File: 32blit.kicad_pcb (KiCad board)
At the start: 4 copper layers, 150 x 65 mm, 121 parts, among them CN1 LIPO BATTERY, J1 1X02PICOBLADE, J3 1X02JST_SH, Q5 DMN3023L, U1 SN74AHC1G02, U11 BQ24295, U22 MT25QL256ABA1EW7-0SIT, U3 AP3031KTR-G1 - ref 200mV, U4 ACCEL_LIS3DHTR, U5 PAM8301, U6 AP2112, U8 74VHC4053AFT, X1 MicroSD

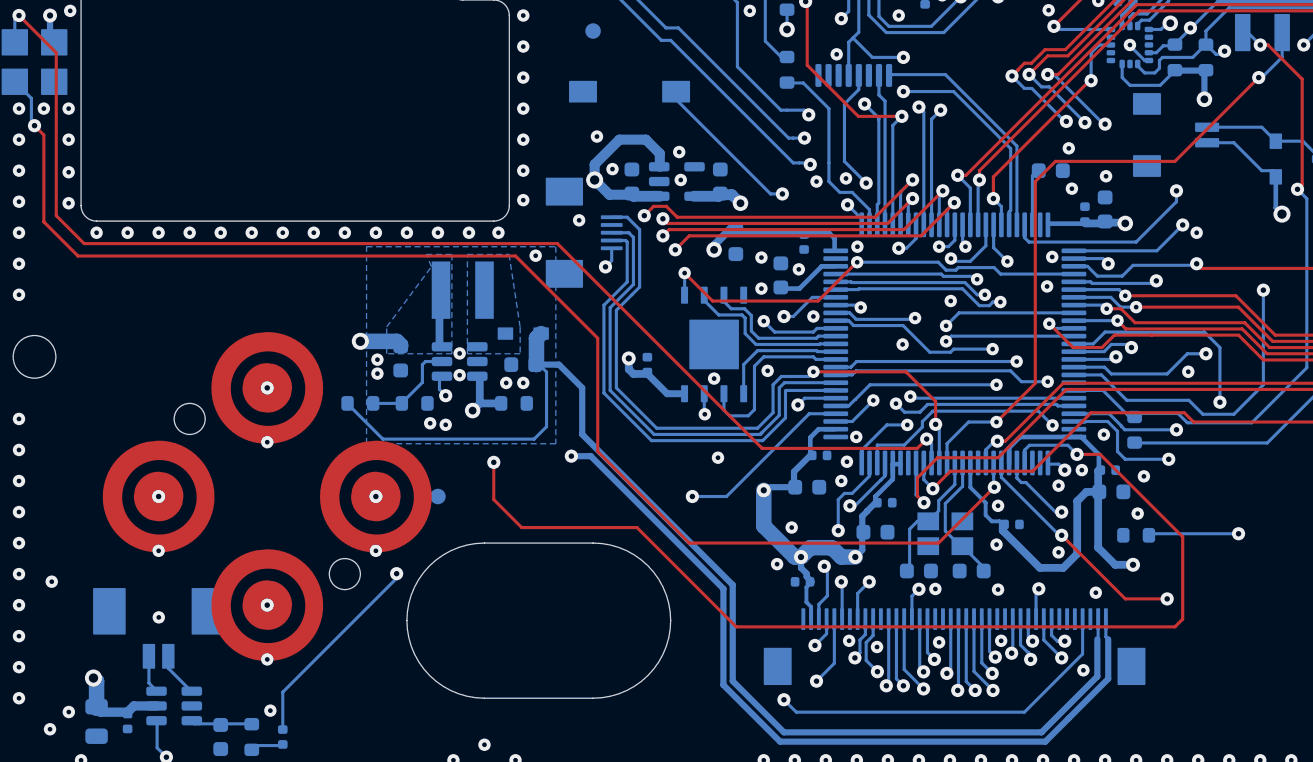
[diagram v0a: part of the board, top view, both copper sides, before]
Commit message: Replace speaker/vibration connector footprints
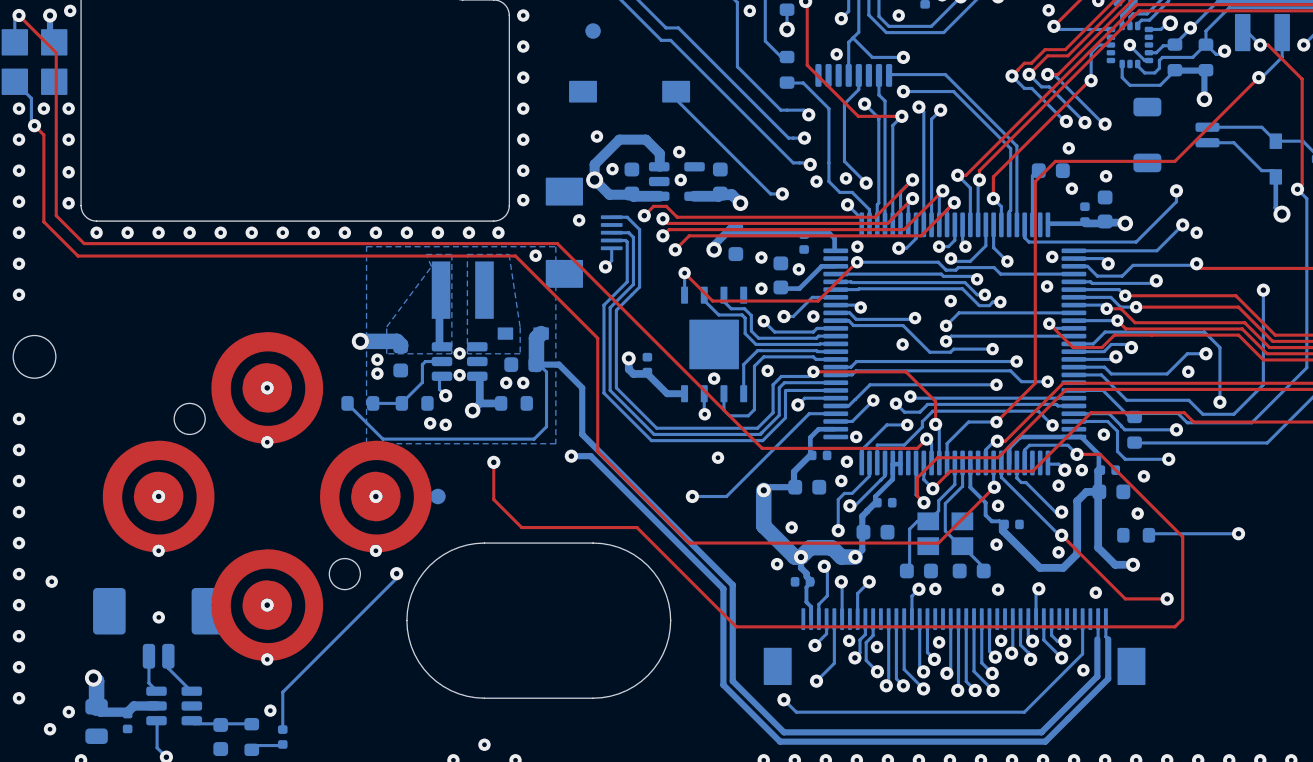
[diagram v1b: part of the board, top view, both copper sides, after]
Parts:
- J1: footprint 32blit:PICOBLADE_1.25MM_2P -> Connector_Molex:Molex_PicoBlade_53261-0271_1x02-1MP_P1.25mm_Horizontal
- J3: footprint 32blit:JST_SH_1.0MM_2P -> Connector_JST:JST_SH_SM02B-SRSS-TB_1x02-1MP_P1.00mm_Horizontal
- moved J3 2.80 mm to (150.1, 91.2)
- moved J1 1.60 mm to (84.5, 122.4)

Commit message: Giant schematic rework
Use as many kicad symbols as possiblem, adjust remaining imported symbols to make ERC happy and adjust some footprints for the new symbols
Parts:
- U4: value ACCEL_LIS3DHTR -> LIS3DHTR
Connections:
- net ACCEL_INT renamed /MCU/ACCEL_INT
- net AJOY_BUTTON renamed /MCU/AJOY_BUTTON
- net AJOY_LR renamed /MCU/AJOY_LR
- net AJOY_UD renamed /MCU/AJOY_UD
- net BATSENSE renamed /LCDs and Power/BATSENSE
- net DAC_AUDIO_OUT renamed /MCU/DAC_AUDIO_OUT
- net DPAD_DOWN renamed /MCU/DPAD_DOWN
- net DPAD_LEFT renamed /MCU/DPAD_LEFT
- net DPAD_RIGHT renamed /MCU/DPAD_RIGHT
- net DPAD_UP renamed /MCU/DPAD_UP
- net FLASH_CS renamed /MCU/FLASH_CS
- net FLASH_D0 renamed /MCU/FLASH_D0
- net FLASH_D1 renamed /MCU/FLASH_D1
- net FLASH_D2 renamed /MCU/FLASH_D2
- net FLASH_D3 renamed /MCU/FLASH_D3
- net FLASH_SCK renamed /MCU/FLASH_SCK
- net LCD_B2 renamed /LCDs and Power/LCD_B2
- net LCD_B3 renamed /LCDs and Power/LCD_B3
- net LCD_B4 renamed /LCDs and Power/LCD_B4
- net LCD_B5 renamed /LCDs and Power/LCD_B5
- net LCD_B6 renamed /LCDs and Power/LCD_B6
- net LCD_B7 renamed /LCDs and Power/LCD_B7
- net LCD_BACKLIGHT_EN renamed /LCDs and Power/LCD_BACKLIGHT_EN
- net LCD_CLK renamed /LCDs and Power/LCD_CLK
- net LCD_CS renamed /LCDs and Power/LCD_CS
- net LCD_DE renamed /LCDs and Power/LCD_DE
- net LCD_G2 renamed /LCDs and Power/LCD_G2
- net LCD_G3 renamed /LCDs and Power/LCD_G3
- net LCD_G4 renamed /LCDs and Power/LCD_G4
- net LCD_G5 renamed /LCDs and Power/LCD_G5
- net LCD_G6 renamed /LCDs and Power/LCD_G6
- net LCD_G7 renamed /LCDs and Power/LCD_G7
- net LCD_HSYNC renamed /LCDs and Power/LCD_HSYNC
- net LCD_R2 renamed /LCDs and Power/LCD_R2
- net LCD_R3 renamed /LCDs and Power/LCD_R3
- net LCD_R4 renamed /LCDs and Power/LCD_R4
- net LCD_R5 renamed /LCDs and Power/LCD_R5
- net LCD_R6 renamed /LCDs and Power/LCD_R6
- net LCD_R7 renamed /LCDs and Power/LCD_R7
- net LCD_RESET renamed /LCDs and Power/LCD_RESET
- net LCD_SPI_MOSI renamed /LCDs and Power/LCD_SPI_MOSI
- net LCD_SPI_SCLK renamed /LCDs and Power/LCD_SPI_SCLK
- net LCD_VSYNC renamed /LCDs and Power/LCD_VSYNC
- net LED_BLUE renamed /MCU/LED_BLUE
- net LED_CHG_BLUE renamed /LCDs and Power/LED_CHG_BLUE
- net LED_CHG_GREEN renamed /LCDs and Power/LED_CHG_GREEN
- net LED_CHG_RED renamed /LCDs and Power/LED_CHG_RED
- net LED_GREEN renamed /MCU/LED_GREEN
- net LED_RED renamed /MCU/LED_RED
- net SD_CS renamed /MCU/SD_CS
- net SD_SPI_MISO renamed /MCU/SD_SPI_MISO
- net SD_SPI_MOSI renamed /MCU/SD_SPI_MOSI
- net SD_SPI_SCLK renamed /MCU/SD_SPI_SCLK
- net SWA renamed /MCU/SWA
- net SWB renamed /MCU/SWB
- net SWHOME renamed /SWHOME
- net SWMENU renamed /MCU/SWMENU
- net VIBE_EN renamed /MCU/VIBE_EN
- net ~{AMP_SD} renamed /MCU/~{AMP_SD}
- C10 pad 1: 3V3 -> +3.3V
- C11 pad 1: 3V3 -> +3.3V
- C17 pad 1: 3V3 -> +3.3V
- C20 pad 1: 3V3 -> +3.3V
- C25 pad 1: 3V3 -> +3.3V
- C26 pad 1: 3V3 -> +3.3V
- C29 pad 1: 3V3 -> +3.3V
- C30 pad 1: 3V3 -> +3.3V
- C32 pad 1: 3V3 -> +3.3V
- C33 pad 1: 3V3 -> +3.3V
- C34 pad 1: 3V3 -> +3.3V
- C39 pad 1: USB_5V -> VBUS
- C4 pad 1: 3V3 -> +3.3V
- C5 pad 1: 3V3 -> +3.3V
- C6 pad 1: 3V3 -> +3.3V
- C7 pad 1: 3V3 -> +3.3V
- C8 pad 1: 3V3 -> +3.3V
- C9 pad 1: 3V3 -> +3.3V
- CN1 pad MP: (no net) -> unconnected-(CN1-MountPin-PadMP)
- FPC2 pad 2: 3V3 -> +3.3V
- J1 pad MP: (no net) -> GND
- J3 pad 1: 3V3 -> +3.3V
- J3 pad 2: Net-(Q5-D) -> Net-(D1-A)
- J3 pad MP: (no net) -> GND
- JOYSTICK0 pad 5: 3V3 -> +3.3V
- L2 pad 2: Net-(U3-SW) -> Net-(D2-A)
- Q5 pad 3: Net-(Q5-D) -> Net-(D1-A)
- R1 pad 2: 3V3 -> +3.3V
- R13 pad 2: 3V3 -> +3.3V
- R19 pad 1: I2C_SCL -> /I2C_SCL
- R19 pad 2: 3V3 -> +3.3V
- R20 pad 1: I2C_SDA -> /I2C_SDA
- R20 pad 2: 3V3 -> +3.3V
- R21 pad 1: USB_5V -> VBUS
- R29 pad 2: 3V3 -> +3.3V
- RGB1 pad 2: 3V3 -> +3.3V
- RGB2 pad 2: 3V3 -> +3.3V
- SJ1 pad 2: USB_5V -> VBUS
- STM32H750 pad 100: 3V3 -> +3.3V
- STM32H750 pad 11: 3V3 -> +3.3V
- STM32H750 pad 20: 3V3 -> +3.3V
- STM32H750 pad 21: 3V3 -> +3.3V
- STM32H750 pad 27: 3V3 -> +3.3V
- STM32H750 pad 50: 3V3 -> +3.3V
- STM32H750 pad 51: USB_ID -> /LCDs and Power/USB_ID
- STM32H750 pad 58: SD_DETECT -> /MCU/SD_DETECT
- STM32H750 pad 59: I2C_SCL -> /I2C_SCL
- STM32H750 pad 6: 3V3 -> +3.3V
- STM32H750 pad 60: I2C_SDA -> /I2C_SDA
- STM32H750 pad 75: 3V3 -> +3.3V
- SWRESET0 pad 2: /MCU/~{RESET} -> GND
- U$19 pad 2: Net-(U$19-GND-Pad2) -> unconnected-(U$19-Pad2)
- U$19 pad 4: Net-(U$19-GND-Pad2) -> unconnected-(U$19-Pad4)
- U1 pad 5: 3V3 -> +3.3V
- U11 pad 1: USB_5V -> VBUS
- U11 pad 2: USB_DP -> /LCDs and Power/USB_DP
- U11 pad 24: USB_5V -> VBUS
- U11 pad 3: USB_DM -> /LCDs and Power/USB_DM
- U11 pad 5: I2C_SCL -> /I2C_SCL
- U11 pad 6: I2C_SDA -> /I2C_SDA
- U22 pad 8: 3V3 -> +3.3V
- U3 pad 1: Net-(U3-SW) -> Net-(D2-A)
- U4 pad 1: 3V3 -> +3.3V
- U4 pad 14: 3V3 -> +3.3V
- U4 pad 4: I2C_SCL -> /I2C_SCL
- U4 pad 6: I2C_SDA -> /I2C_SDA
- U4 pad 8: 3V3 -> +3.3V
- U6 pad 4: (no net) -> unconnected-(U6-NC-Pad4)
- U6 pad 5: 3V3 -> +3.3V
- U8 pad 14: USB_DM -> /LCDs and Power/USB_DM
- U8 pad 15: USB_DP -> /LCDs and Power/USB_DP
- U8 pad 16: 3V3 -> +3.3V
- X1 pad 4: 3V3 -> +3.3V
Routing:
- net 3V3: track 145.6 -> 0.00 mm, vias 24 -> 0
- net +3.3V: track 0.00 -> 145.6 mm, vias 0 -> 24
- net VBUS: track 0.00 -> 85.1 mm, vias 0 -> 2
- net USB_5V: track 85.1 -> 0.00 mm, vias 2 -> 0
- net I2C_SDA: track 74.7 -> 0.00 mm, vias 4 -> 0
- net /I2C_SDA: track 0.00 -> 74.7 mm, vias 0 -> 4
- net I2C_SCL: track 71.3 -> 0.00 mm, vias 4 -> 0
- net /I2C_SCL: track 0.00 -> 71.3 mm, vias 0 -> 4
- net USB_DM: track 66.0 -> 0.00 mm
- net /LCDs and Power/USB_DM: track 0.00 -> 66.0 mm
- net USB_DP: track 65.0 -> 0.00 mm, vias 2 -> 0
- net /LCDs and Power/USB_DP: track 0.00 -> 65.0 mm, vias 0 -> 2
- net USB_ID: track 35.6 -> 0.00 mm, vias 2 -> 0
- net /LCDs and Power/USB_ID: track 0.00 -> 35.6 mm, vias 0 -> 2
- net SD_DETECT: track 21.2 -> 0.00 mm, vias 2 -> 0
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- added copper zone on In1.Cu, net +3.3V
- added copper zone on B.Cu, net Net-(D2-A)
- added copper zone on B.Cu, net VBUS
- removed copper zone on In1.Cu, net 3V3
- removed copper zone on B.Cu, net Net-(U3-SW)
- removed copper zone on B.Cu, net USB_5V

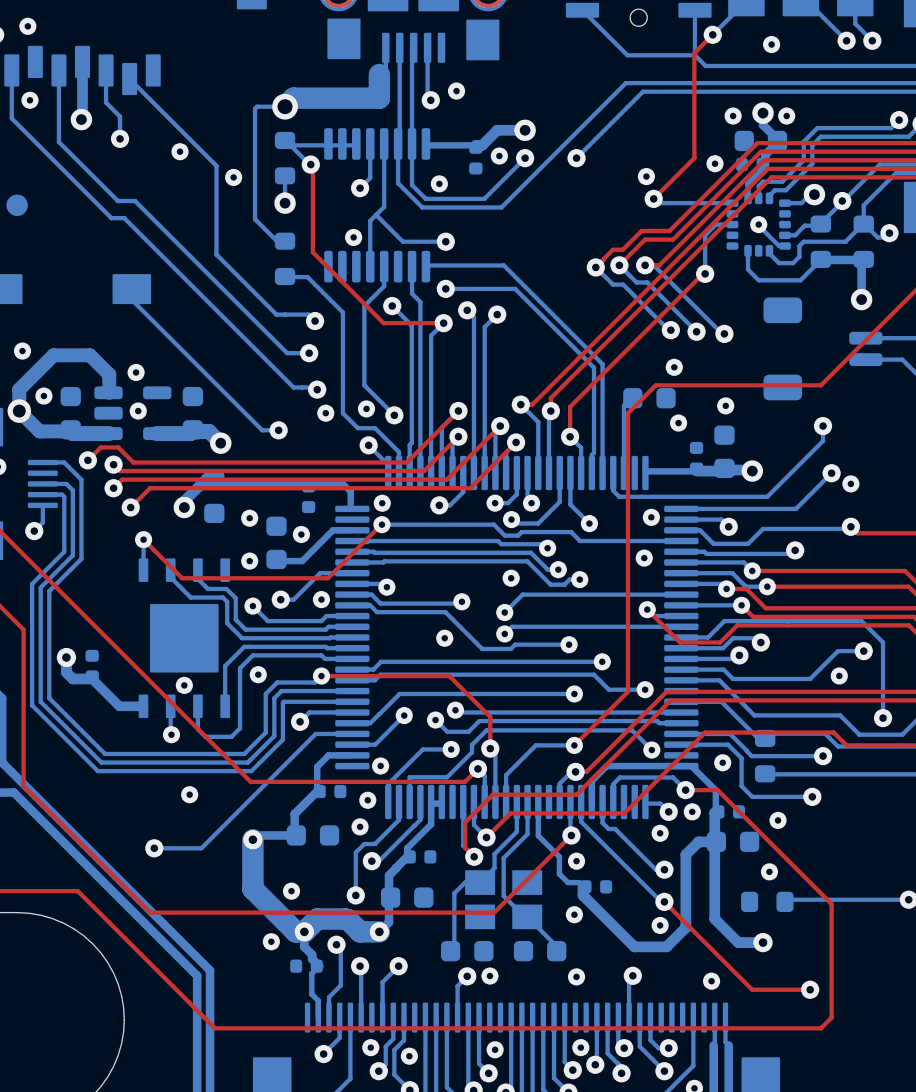
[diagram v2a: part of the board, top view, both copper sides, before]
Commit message: Some board/footprint fixes
The holes were violating their own keepout. Also adjust some clearances and move a few capacitors a little
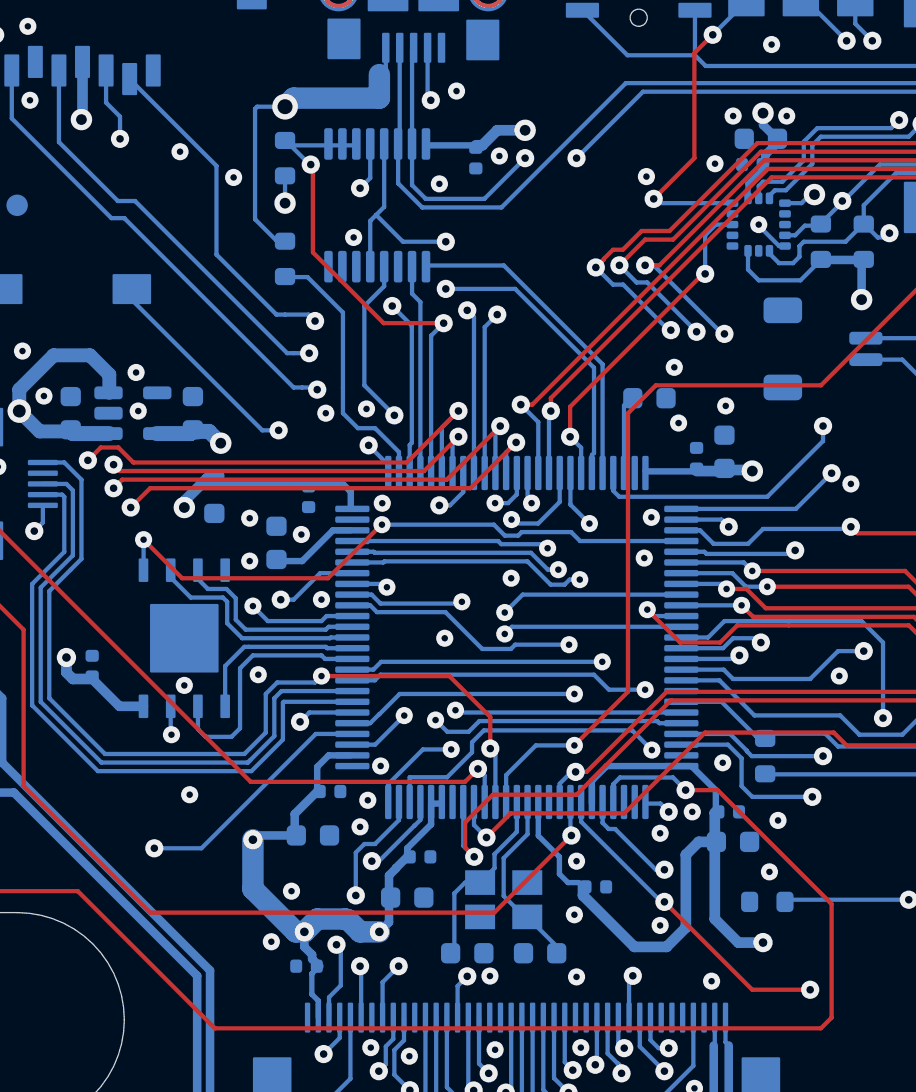
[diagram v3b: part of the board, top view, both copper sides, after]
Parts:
- moved C17 0.10 mm to (147.2, 81.4)
- moved C24 0.10 mm to (136.9, 119.4)
- moved C35 0.10 mm to (133.5, 119.4)
